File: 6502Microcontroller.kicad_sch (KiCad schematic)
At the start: 33 parts, among them IC1 W65C02S6TPG-14, IC3 AT28HC256E-90SU, IC4 AS6C62256-55PCN, J10 Barrel_Jack, J11 Conn_02x02_Counter_Clockwise, J12 ~{IRQ}_SW, J9 USB_C_Receptacle_PowerOnly_6P, SW2 SW_Push, Y1 4MHz, Y2 1.8432 MHz

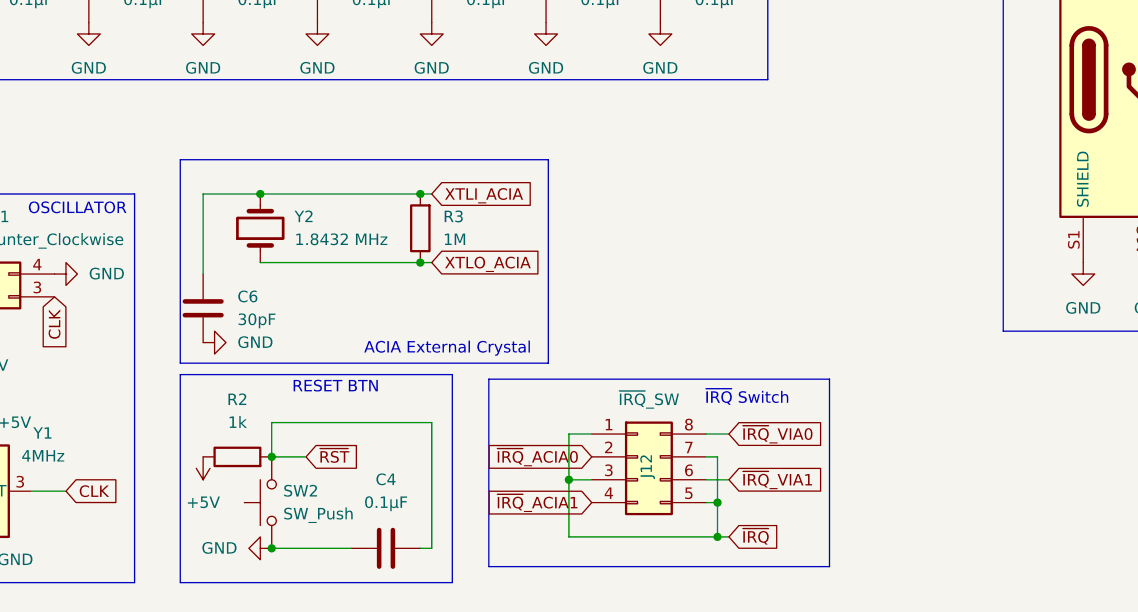
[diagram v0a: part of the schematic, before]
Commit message: add reset supervisor ic
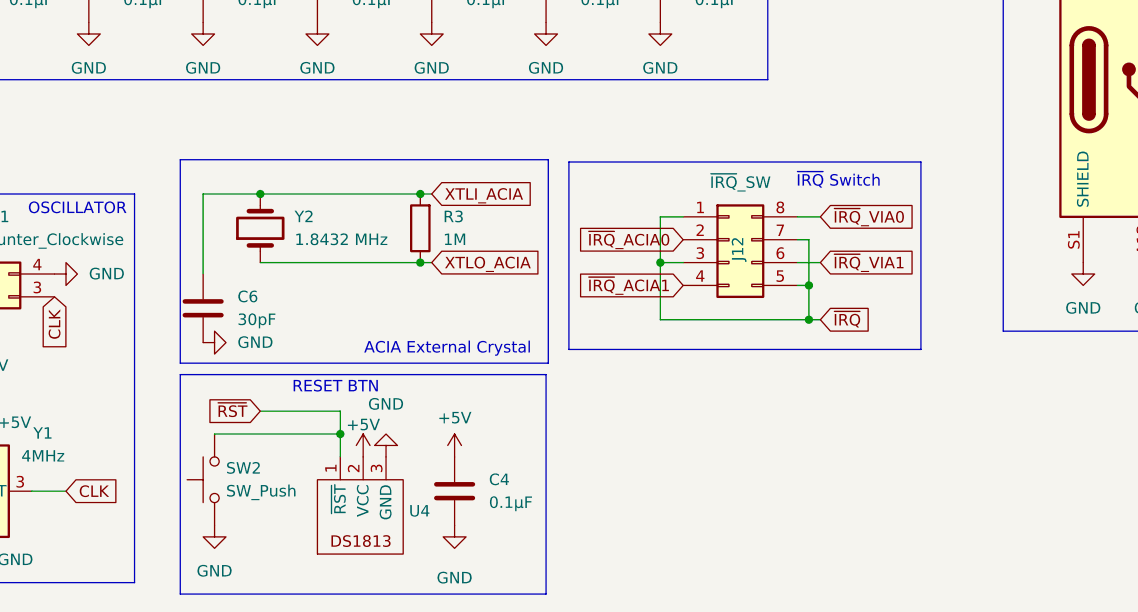
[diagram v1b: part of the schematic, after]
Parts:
- removed R2: 1k, Resistor_SMD:R_0603_1608Metric_Pad0.98x0.95mm_HandSolder, symbol Device:R
- added U4: ~, LCSCLib:SOT-23-3_L2.9-W1.3-P1.90-LS2.4-BR, symbol LCSCLib:DS1813R
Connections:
- net +5V: now also C4.2, U4.2 (VCC)
- net GND: now also U4.3 (GND)
- net ~{RST}: now also U4.1 (~{RST}); no longer C4.2
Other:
- moved on the sheet: C4, J12, SW2

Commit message: feat: add proper headers
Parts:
- J11: footprint Connector_PinSocket_2.54mm:PinSocket_2x02_P2.54mm_Vertical_SMD -> LCSCLib:HDR-TH_4P-P2.54-V-F-R2-C2-S2.54
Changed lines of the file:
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@@
 	(wire
 		(pts
-			(xy 31.75 44.45) (xy 33.02 44.45)
-		)
-		(stroke
-			(width 0)
-			(type default)
-		)
-	)
-	(wire
-		(pts
 			(xy 152.4 45.72) (xy 154.94 45.72)
 		)
@@
 	)
 	(symbol
+		(lib_id "power:+5V")
+		(at 33.02 44.45 90)
+		(unit 1)
+		(exclude_from_sim no)
+		(in_bom yes)
+		(on_board yes)
+		(dnp no)
+		(property "Reference" "#PWR02"
+			(at 36.83 44.45 0)
+			(effects
+				(font
+					(size 1.27 1.27)
+				)
+				(hide yes)
+			)
+		)
+		(property "Value" "+5V"
+			(at 30.226 43.688 90)
+			(effects
+				(font
+					(size 1.27 1.27)
+				)
+				(justify left)
+			)
+		)
+		(property "Footprint" ""
+			(at 33.02 44.45 0)
+			(effects
+				(font
+					(size 1.27 1.27)
+				)
+				(hide yes)
+			)
+		)
+		(property "Datasheet" ""
+			(at 33.02 44.45 0)
+			(effects
+				(font
+					(size 1.27 1.27)
+				)
+				(hide yes)
+			)
+		)
+		(property "Description" "Power symbol creates a global label with name \"+5V\""
+			(at 33.02 44.45 0)
+			(effects
+				(font
+					(size 1.27 1.27)
+				)
+				(hide yes)
+			)
+		)
+		(pin "1"
+		)
+		(instances
+			(project "6502Microcontroller"
+				(path "/18e16338-affd-4f01-bda8-cdea79e76b9f"
+					(reference "#PWR02")
+					(unit 1)
+				)
+			)
+		)
+	)
+	(symbol
 		(lib_id "Device:C")
 		(at 261.62 148.59 270)
@@
 			)
 		)
-		(property "Footprint" "Connector_PinSocket_2.54mm:PinSocket_2x02_P2.54mm_Vertical_SMD"
+		(property "Footprint" "LCSCLib:HDR-TH_4P-P2.54-V-F-R2-C2-S2.54"
 			(at 64.77 158.75 0)
 			(effects
@@
 	)
 	(symbol
-		(lib_id "power:+5V")
-		(at 31.75 44.45 90)
-		(unit 1)
-		(exclude_from_sim no)
-		(in_bom yes)
-		(on_board yes)
-		(dnp no)
-		(fields_autoplaced yes)
-		(property "Reference" "#PWR02"
-			(at 35.56 44.45 0)
-			(effects
-				(font
-					(size 1.27 1.27)
-				)
-				(hide yes)
-			)
-		)
-		(property "Value" "+5V"
-			(at 27.94 44.4499 90)
-			(effects
-				(font
-					(size 1.27 1.27)
-				)
-				(justify left)
-			)
-		)
-		(property "Footprint" ""
-			(at 31.75 44.45 0)
-			(effects
-				(font
-					(size 1.27 1.27)
-				)
-				(hide yes)
-			)
-		)
-		(property "Datasheet" ""
-			(at 31.75 44.45 0)
-			(effects
-				(font
-					(size 1.27 1.27)
-				)
-				(hide yes)
-			)
-		)
-		(property "Description" "Power symbol creates a global label with name \"+5V\""
-			(at 31.75 44.45 0)
-			(effects
-				(font
-					(size 1.27 1.27)
-				)
-				(hide yes)
-			)
-		)
-		(pin "1"
-		)
-		(instances
-			(project ""
-				(path "/18e16338-affd-4f01-bda8-cdea79e76b9f"
-					(reference "#PWR02")
-					(unit 1)
-				)
-			)
-		)
-	)
-	(symbol
 		(lib_id "power:GND")
 		(at 101.6 130.81 0)
@@
 		(on_board yes)
 		(dnp no)
-		(fields_autoplaced yes)
 		(property "Reference" "#PWR08"
 			(at 36.83 39.37 0)
@@
 		)
 		(property "Value" "+5V"
-			(at 29.21 39.3699 90)
+			(at 30.226 38.608 90)
 			(effects
 				(font
